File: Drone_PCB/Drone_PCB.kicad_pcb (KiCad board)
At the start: 2 copper layers, 27 parts, among them Q1 BSS214NW, Q2 BSS214NW, U1 STM32F411RCT6, U2 AP2112K-3.3, U3 TP4056-42-ESOP8, U4 DW01A

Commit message: Creating PCB part 1
Circuit is looking pretty neat
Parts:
- added J1: Conn_01x04_Pin, Connector_PinHeader_2.54mm:PinHeader_1x04_P2.54mm_Vertical, F.Cu at (113.5, 53.2)
- added J2: Conn_01x04_Pin, Connector_PinHeader_2.54mm:PinHeader_1x04_P2.54mm_Vertical, F.Cu at (118.1, 53.2)
- added J3: Conn_01x04_Pin, Connector_PinHeader_2.54mm:PinHeader_1x04_P2.54mm_Vertical, F.Cu at (122.7, 53.2)
- added J4: Conn_01x06_Pin, Connector_PinHeader_2.54mm:PinHeader_1x06_P2.54mm_Vertical, F.Cu at (124.4, 73.3)
- added J5: Conn_01x06_Pin, Connector_PinHeader_2.54mm:PinHeader_1x06_P2.54mm_Vertical, F.Cu at (129.0, 73.3)
- added J6: USB_B_Micro, Connector_USB:USB_Micro-B_Wuerth_629105150521, F.Cu at (116.6, 74.9)
- added R1: 10k, Resistor_SMD:R_0402_1005Metric, F.Cu at (112.6, 81.2)
- added R2: 1k5, Resistor_SMD:R_0402_1005Metric, F.Cu at (112.6, 83.2)
- added R3: 1k5, Resistor_SMD:R_0402_1005Metric, F.Cu at (112.6, 85.2)
- added R4: 1k5, Resistor_SMD:R_0402_1005Metric, F.Cu at (115.5, 81.2)
- added R5: 1.2k, Resistor_SMD:R_0402_1005Metric, F.Cu at (115.5, 83.2)
- added R6: 100, Resistor_SMD:R_0402_1005Metric, F.Cu at (115.5, 85.2)
- added R7: 1k, Resistor_SMD:R_0402_1005Metric, F.Cu at (118.5, 81.2)
- added R8: 1k, Resistor_SMD:R_0402_1005Metric, F.Cu at (118.5, 83.2)
- added R9: 1k, Resistor_SMD:R_0402_1005Metric, F.Cu at (118.5, 85.2)
- added SW2: SW_DPST_x2, Button_Switch_THT:SW_E-Switch_EG1224_SPDT_Angled, F.Cu at (99.4, 54.5)
- added Y1: 26MHz, Crystal:Crystal_SMD_HC49-SD, F.Cu at (36.5, 47.8)
- moved C6 130.6 mm to (133.3, 72.3)
- moved FB1 130.6 mm to (133.3, 74.8)
- moved D1 130.3 mm to (133.2, 64.4)
- moved D2 130.3 mm to (133.2, 67.0)
- moved D3 130.3 mm to (133.2, 69.6)
- moved U3 126.0 mm to (126.9, 66.5)
- moved C10 122.0 mm to (118.3, 64.1)
- moved C13 122.0 mm to (118.3, 70.0)
- moved C14 122.0 mm to (121.2, 64.1)
- moved C15 122.0 mm to (121.2, 66.1)
- moved C16 122.0 mm to (121.2, 68.0)
- moved C17 122.0 mm to (121.2, 70.0)
- moved C7 122.0 mm to (115.5, 66.1)
- moved C8 122.0 mm to (115.5, 68.0)
- moved C9 122.0 mm to (115.5, 70.0)
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
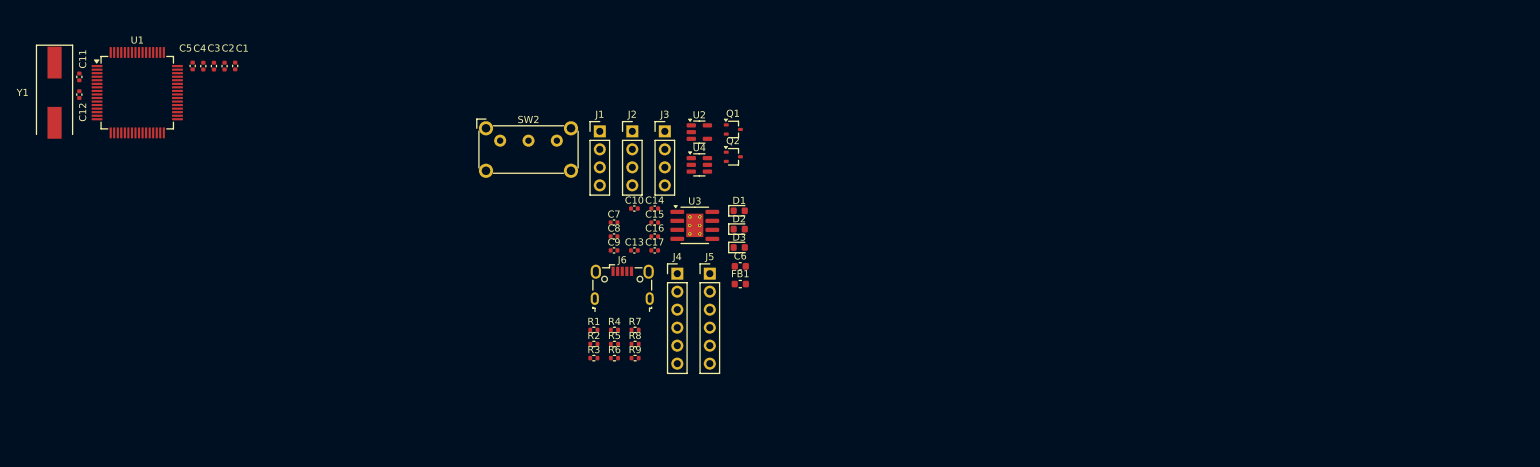
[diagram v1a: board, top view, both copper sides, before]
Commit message: PCB #1
MCU, Decoupling Capacitors and Crystal layout
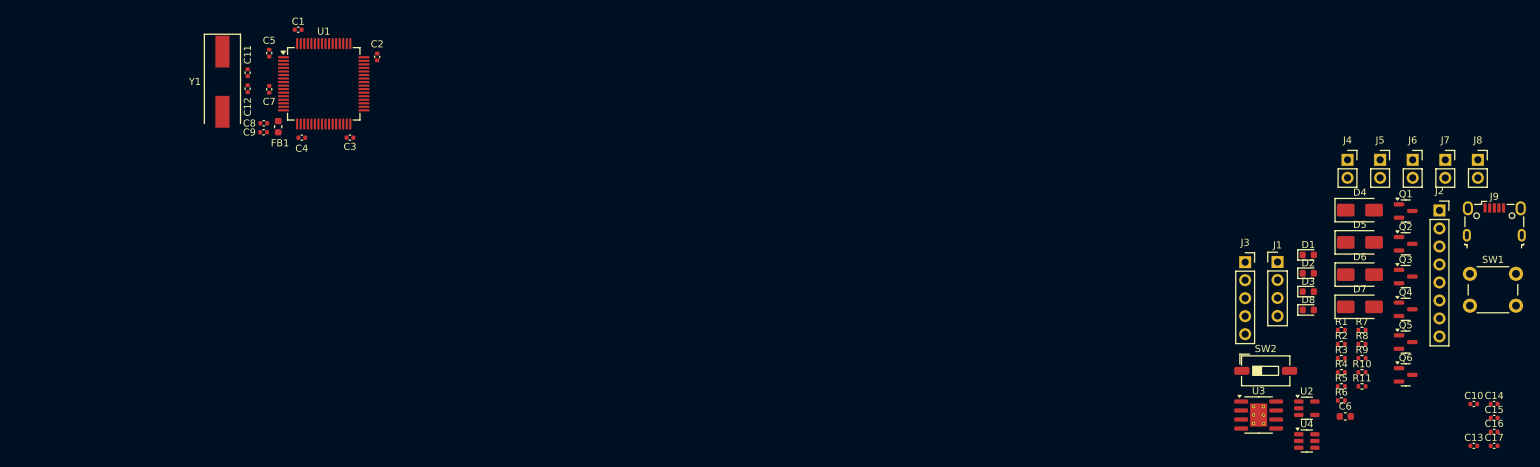
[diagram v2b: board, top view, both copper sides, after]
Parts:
- added D4: SS14, Diode_SMD:D_SMA, F.Cu at (220.8, 64.3)
- added D5: SS14, Diode_SMD:D_SMA, F.Cu at (220.8, 68.9)
- added D6: SS14, Diode_SMD:D_SMA, F.Cu at (220.8, 73.4)
- added D7: SS14, Diode_SMD:D_SMA, F.Cu at (220.8, 78.0)
- added D8: YELLOW_LED, LED_SMD:LED_0603_1608Metric, F.Cu at (213.5, 78.4)
- added J7: Conn_01x02_Socket, Connector_PinSocket_2.54mm:PinSocket_1x02_P2.54mm_Vertical, F.Cu at (232.8, 57.2)
- added J8: Conn_01x02_Socket, Connector_PinSocket_2.54mm:PinSocket_1x02_P2.54mm_Vertical, F.Cu at (237.4, 57.2)
- added J9: USB_B_Micro, Connector_USB:USB_Micro-B_Wuerth_629105150521, F.Cu at (239.7, 65.9)
- added Q3: AO3400A, Package_TO_SOT_SMD:SOT-23, F.Cu at (227.2, 73.7)
- added Q4: AO3400A, Package_TO_SOT_SMD:SOT-23, F.Cu at (227.2, 78.3)
- added Q5: AO3400A, Package_TO_SOT_SMD:SOT-23, F.Cu at (227.2, 83.0)
- added Q6: AO3400A, Package_TO_SOT_SMD:SOT-23, F.Cu at (227.2, 87.6)
- added R10: 10k, Resistor_SMD:R_0402_1005Metric, F.Cu at (221.1, 87.2)
- added R11: 220, Resistor_SMD:R_0402_1005Metric, F.Cu at (221.1, 89.2)
- added SW1: SW_Push, Button_Switch_THT:SW_PUSH_6mm, F.Cu at (236.3, 73.3)
- J2: value Conn_01x04_Pin -> Conn_01x08_Socket; footprint Connector_PinHeader_2.54mm:PinHeader_1x04_P2.54mm_Vertical -> Connector_PinSocket_2.54mm:PinSocket_1x08_P2.54mm_Vertical
- J3: value Conn_01x04_Pin -> Conn_01x05_Socket; footprint Connector_PinHeader_2.54mm:PinHeader_1x04_P2.54mm_Vertical -> Connector_PinSocket_2.54mm:PinSocket_1x05_P2.54mm_Vertical
- J4, J5: value Conn_01x06_Pin -> Conn_01x02_Socket; footprint Connector_PinHeader_2.54mm:PinHeader_1x06_P2.54mm_Vertical -> Connector_PinSocket_2.54mm:PinSocket_1x02_P2.54mm_Vertical
- J6: value USB_B_Micro -> Conn_01x02_Socket; footprint Connector_USB:USB_Micro-B_Wuerth_629105150521 -> Connector_PinSocket_2.54mm:PinSocket_1x02_P2.54mm_Vertical
- Q1, Q2: value BSS214NW -> AO3400A; footprint Package_TO_SOT_SMD:SOT-323_SC-70 -> Package_TO_SOT_SMD:SOT-23
- SW2: value SW_DPST_x2 -> SW_SPST; footprint Button_Switch_THT:SW_E-Switch_EG1224_SPDT_Angled -> Button_Switch_SMD:SW_DIP_SPSTx01_Slide_6.7x4.1mm_W6.73mm_P2.54mm_LowProfile_JPin
- moved C10 121.7 mm to (236.8, 91.7)
- moved C13 121.7 mm to (236.8, 97.6)
- moved C14 121.7 mm to (239.7, 91.7)
- moved C15 121.7 mm to (239.7, 93.7)
- moved C16 121.7 mm to (239.7, 95.6)
- moved C17 121.7 mm to (239.7, 97.6)
- moved J2 114.5 mm to (232.0, 64.4)
- moved J6 113.0 mm to (228.2, 57.2)
- moved SW2 112.8 mm to (207.5, 87.0)
- moved R1 105.5 mm to (218.2, 81.2)
- moved R2 105.5 mm to (218.2, 83.2)
- moved R3 105.5 mm to (218.2, 85.2)
- moved R4 102.8 mm to (218.2, 87.2)
- moved R5 102.8 mm to (218.2, 89.2)
- moved R6 102.8 mm to (218.2, 91.2)
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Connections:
- net /UART_RX renamed /TX
- net /UART_TX renamed /RX
- C17 pad 1: VCC -> +3.3V
- D2 pad 2: VCC -> VBUS
- D3 pad 2: VCC -> VBUS
- J2 pad 1: GND -> /INT
- J2 pad 2: /I2C_SDA -> /ADO
- J2 pad 3: /I2C_SCL -> /XCL
- J2 pad 4: +3.3V -> /XDA
- J3 pad 1: GND -> +3.3V
- J3 pad 4: +3.3V -> GND
- J4 pad 1: GND -> +3.3V
- J4 pad 2: /MOTOR_RB -> Net-(D4-A)
- J5 pad 2: /LED_SIGNAL -> Net-(D5-A)
- J6 pad 1: VBUS -> +3.3V
- J6 pad 2: unconnected-(J6-D--Pad2) -> Net-(D6-A)
- R3 pad 2: /I2C_SCL -> /SCL
- R4 pad 2: /I2C_SDA -> /SDA
- R6 pad 2: VCC -> +3.3V
- SW2 pad 1: VCC -> +3.3V
- U1 pad 58: /I2C_SCL -> /SCL
- U1 pad 59: /I2C_SDA -> /SDA
- U3 pad 5: VCC -> +3.3V

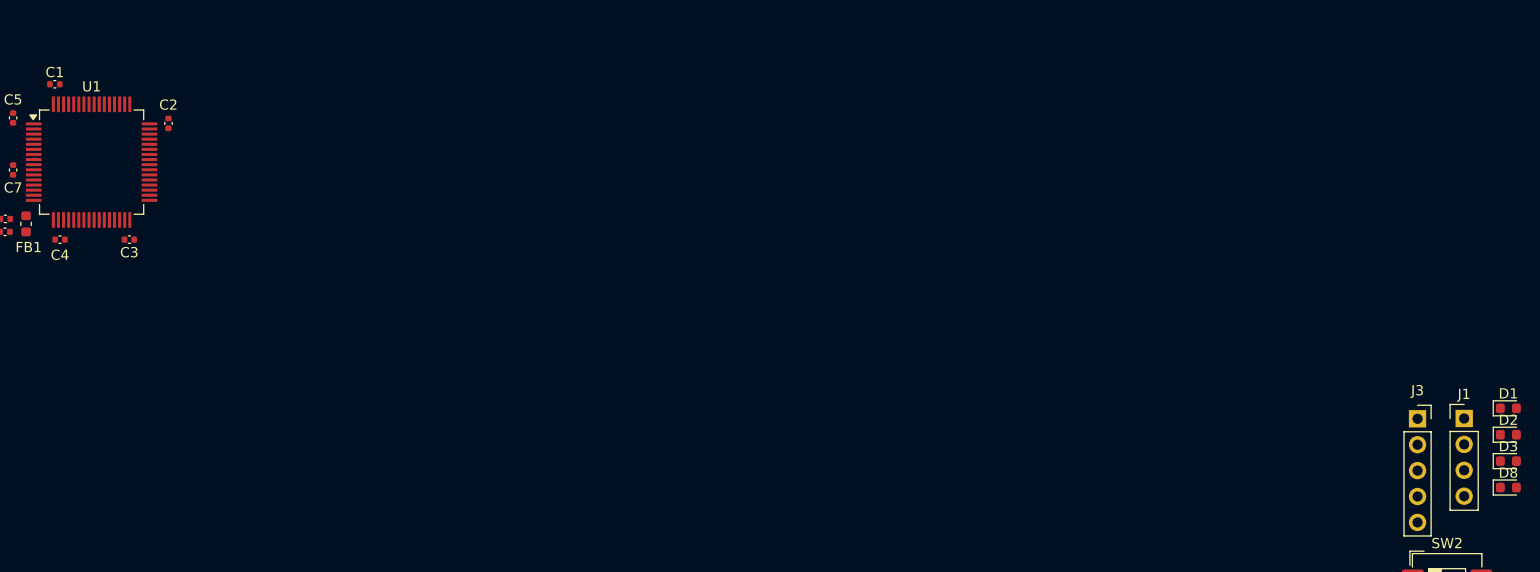
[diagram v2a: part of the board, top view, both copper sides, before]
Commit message: SWD Layout
Added SWD pinout
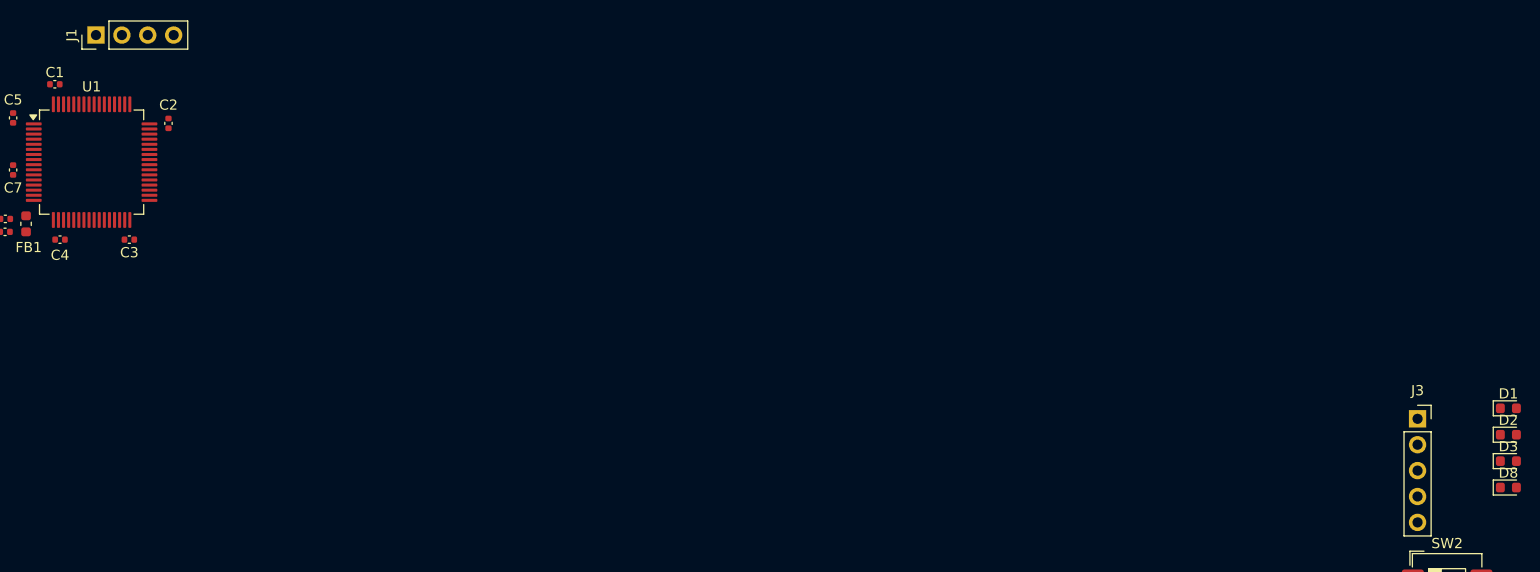
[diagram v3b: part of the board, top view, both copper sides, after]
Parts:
- moved J1 139.4 mm to (74.9, 34.0), turned to 90 degrees
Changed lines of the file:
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@@
 	(footprint "Connector_PinHeader_2.54mm:PinHeader_1x04_P2.54mm_Vertical"
 		(layer "F.Cu")
-		(at 209.14 71.65)
+		(at 74.93 34.036 90)
 		(descr "Through hole straight pin header, 1x04, 2.54mm pitch, single row")
 		(tags "Through hole pin header THT 1x04 2.54mm single row")
 		(property "Reference" "J1"
-			(at 0 -2.38 0)
+			(at 0 -2.38 90)
 			(layer "F.SilkS")
 			(effects
@@
 		)
 		(property "Value" "Conn_01x04_Pin"
-			(at 0 10 0)
+			(at 0 10 90)
 			(layer "F.Fab")
 			(effects
@@
 		)
 		(property "Datasheet" ""
-			(at 0 0 0)
+			(at 0 0 90)
 			(layer "F.Fab")
 			(hide yes)
@@
 		)
 		(property "Description" "Generic connector, single row, 01x04, script generated"
-			(at 0 0 0)
+			(at 0 0 90)
 			(layer "F.Fab")
 			(hide yes)
@@
 		)
 		(fp_line
+			(start 1.38 1.27)
+			(end 1.38 9)
+			(stroke
+				(width 0.12)
+				(type solid)
+			)
+			(layer "F.SilkS")
+		)
+		(fp_line
+			(start -1.38 1.27)
+			(end 1.38 1.27)
+			(stroke
+				(width 0.12)
+				(type solid)
+			)
+			(layer "F.SilkS")
+		)
+		(fp_line
 			(start -1.38 1.27)
 			(end -1.38 9)
@@
 		)
 		(fp_line
-			(start -1.38 1.27)
-			(end 1.38 1.27)
-			(stroke
-				(width 0.12)
-				(type solid)
-			)
-			(layer "F.SilkS")
-		)
-		(fp_line
 			(start -1.38 9)
 			(end 1.38 9)
@@
 		)
 		(fp_line
-			(start 1.38 1.27)
-			(end 1.38 9)
-			(stroke
-				(width 0.12)
-				(type solid)
-			)
-			(layer "F.SilkS")
+			(start 1.77 -1.77)
+			(end -1.77 -1.77)
+			(stroke
+				(width 0.05)
+				(type solid)
+			)
+			(layer "F.CrtYd")
 		)
 		(fp_line
@@
 		)
 		(fp_line
+			(start 1.77 9.39)
+			(end 1.77 -1.77)
+			(stroke
+				(width 0.05)
+				(type solid)
+			)
+			(layer "F.CrtYd")
+		)
+		(fp_line
 			(start -1.77 9.39)
 			(end 1.77 9.39)
@@
 		)
 		(fp_line
-			(start 1.77 -1.77)
-			(end -1.77 -1.77)
-			(stroke
-				(width 0.05)
-				(type solid)
-			)
-			(layer "F.CrtYd")
-		)
-		(fp_line
-			(start 1.77 9.39)
-			(end 1.77 -1.77)
-			(stroke
-				(width 0.05)
-				(type solid)
-			)
-			(layer "F.CrtYd")
+			(start 1.27 -1.27)
+			(end 1.27 8.89)
+			(stroke
+				(width 0.1)
+				(type solid)
+			)
+			(layer "F.Fab")
+		)
+		(fp_line
+			(start -0.635 -1.27)
+			(end 1.27 -1.27)
+			(stroke
+				(width 0.1)
+				(type solid)
+			)
+			(layer "F.Fab")
 		)
 		(fp_line
@@
 		)
 		(fp_line
+			(start 1.27 8.89)
+			(end -1.27 8.89)
+			(stroke
+				(width 0.1)
+				(type solid)
+			)
+			(layer "F.Fab")
+		)
+		(fp_line
 			(start -1.27 8.89)
 			(end -1.27 -0.635)
@@
 			(layer "F.Fab")
 		)
-		(fp_line
-			(start -0.635 -1.27)
-			(end 1.27 -1.27)
-			(stroke
-				(width 0.1)
-				(type solid)
-			)
-			(layer "F.Fab")
-		)
-		(fp_line
-			(start 1.27 -1.27)
-			(end 1.27 8.89)
-			(stroke
-				(width 0.1)
-				(type solid)
-			)
-			(layer "F.Fab")
-		)
-		(fp_line
-			(start 1.27 8.89)
-			(end -1.27 8.89)
-			(stroke
-				(width 0.1)
-				(type solid)
-			)
-			(layer "F.Fab")
-		)
 		(fp_text user "${REFERENCE}"
-			(at 0 3.81 90)
+			(at 0 3.81 0)
 			(layer "F.Fab")
 			(effects
@@
 		)
 		(pad "1" thru_hole rect
-			(at 0 0)
+			(at 0 0 90)
 			(size 1.7 1.7)
 			(drill 1)
@@
 		)
 		(pad "2" thru_hole circle
-			(at 0 2.54)
+			(at 0 2.54 90)
 			(size 1.7 1.7)
 			(drill 1)
@@
 		)
 		(pad "3" thru_hole circle
-			(at 0 5.08)
+			(at 0 5.08 90)
 			(size 1.7 1.7)
 			(drill 1)
@@
 		)
 		(pad "4" thru_hole circle
-			(at 0 7.62)
-			(size 1.7 1.7)
-			(drill 1)
+			(at 0 7.62 90)
+			(size 1.7 1.7)
+			(drill 1)
